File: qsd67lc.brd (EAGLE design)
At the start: 160 x 100 mm, 31 parts, among them IC1 MEGA8-P, IC2 BTS555E3146, Q2 IRLZ44Z, U1 HC_05

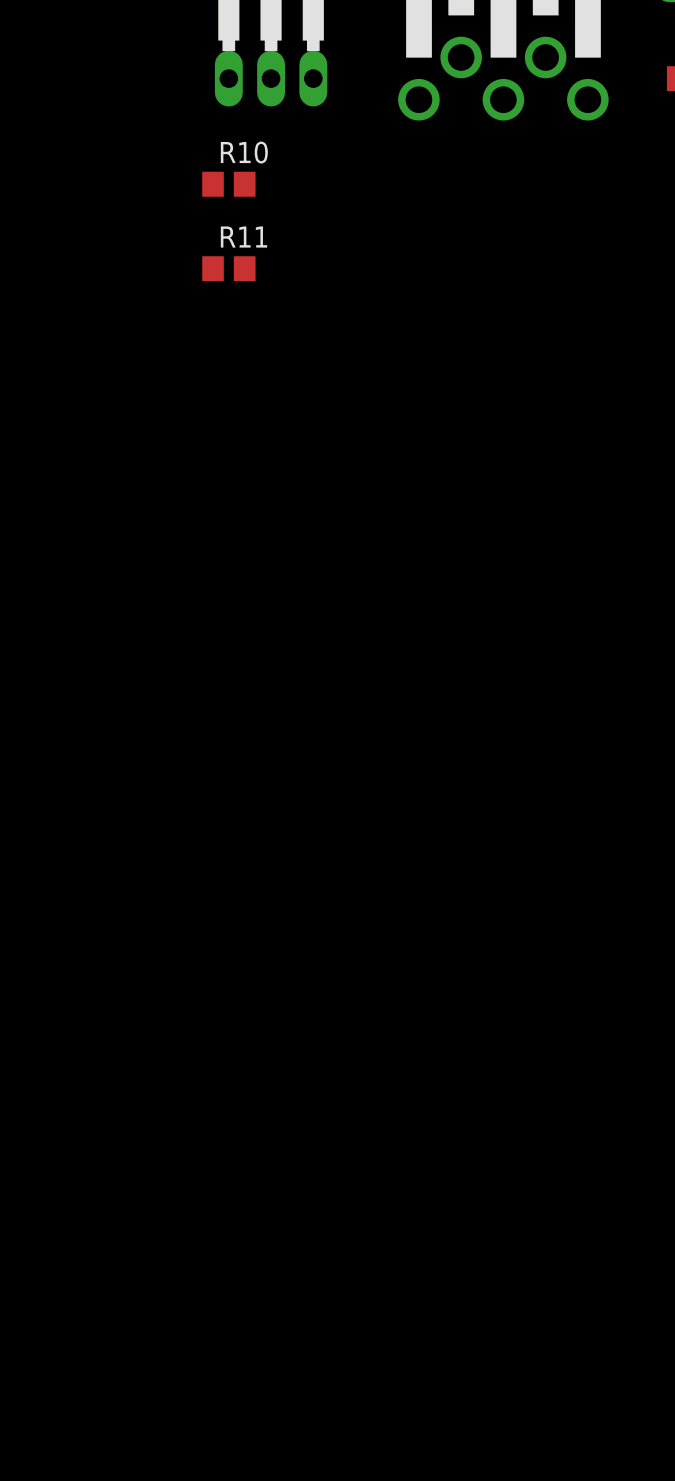
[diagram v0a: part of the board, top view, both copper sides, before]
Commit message: added rs232 for direct PC communication
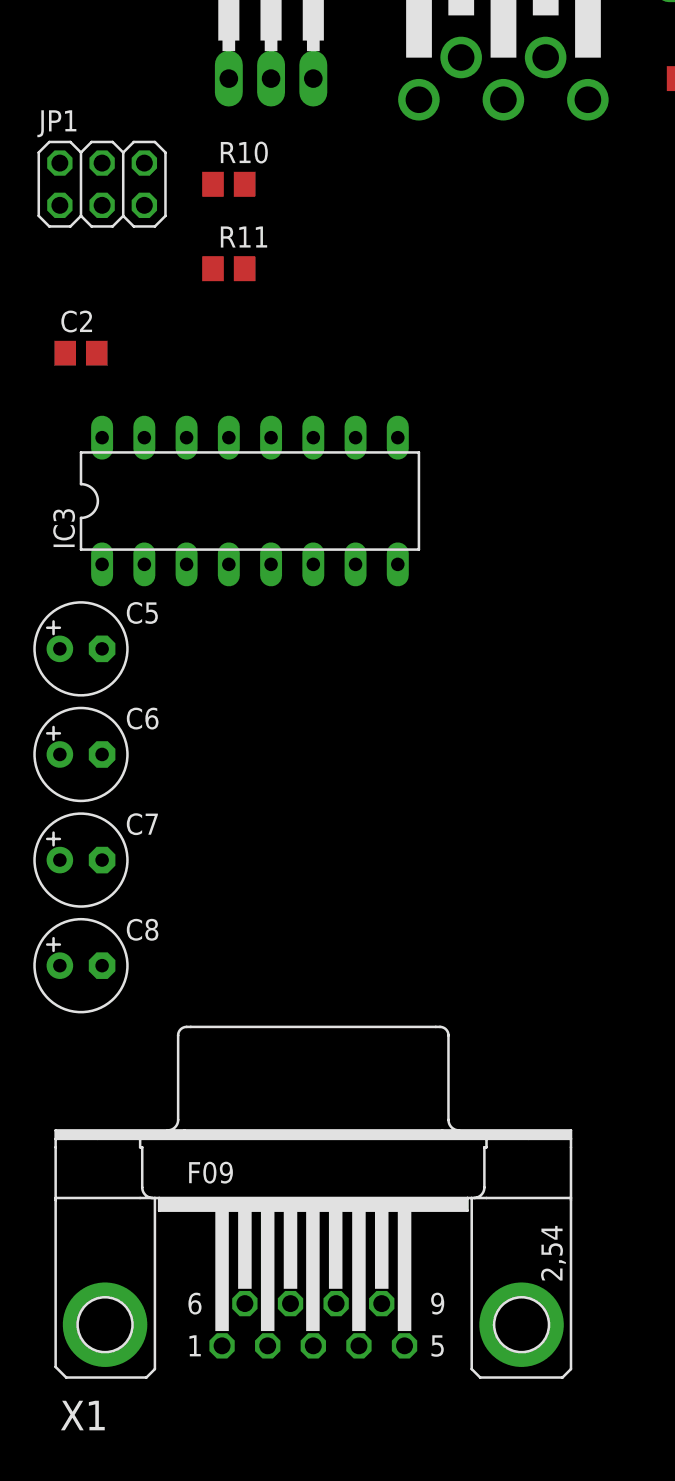
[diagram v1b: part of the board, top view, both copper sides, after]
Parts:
- added C2: 100n, rcl:C0805
- added C5, C6, C7, C8: (no value), rcl:E2,5-6
- added IC3: MAX3232CPE, maxim:DIL16
- added JP1: UART_SELECTOR, pinhead:2X03
- added X1: RS232, con-subd:F09HP
- R10, R11: value (none) -> 10k
- R5, R6: value 220 -> 10k
- SV1: value (none) -> ISP
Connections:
- new net N$11: C7.+, IC3.2
- new net N$15: C8.-, IC3.6
- new net N$17: C5.+, IC3.1
- new net N$18: C6.+, IC3.4
- new net N$19: C6.-, IC3.5
- new net N$20: C5.-, IC3.3
- new net RS232_RX: IC3.14, X1.2
- new net RS232_TX: IC3.13, X1.3
- new net RXD_BT: JP1.1, U1.1
- new net RXD_RS232: IC3.12, JP1.5
- new net TXD_BT: JP1.2, U1.2
- new net TXD_RS232: IC3.11, JP1.6
- net +3V3: now also C2.1, IC3.16
- net GND: now also C2.2, C7.-, C8.+, IC3.15, X1.1, X1.5
- net RXD: now also JP1.3
- net TXD: now also JP1.4
